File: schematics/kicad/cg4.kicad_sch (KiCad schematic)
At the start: 0 parts

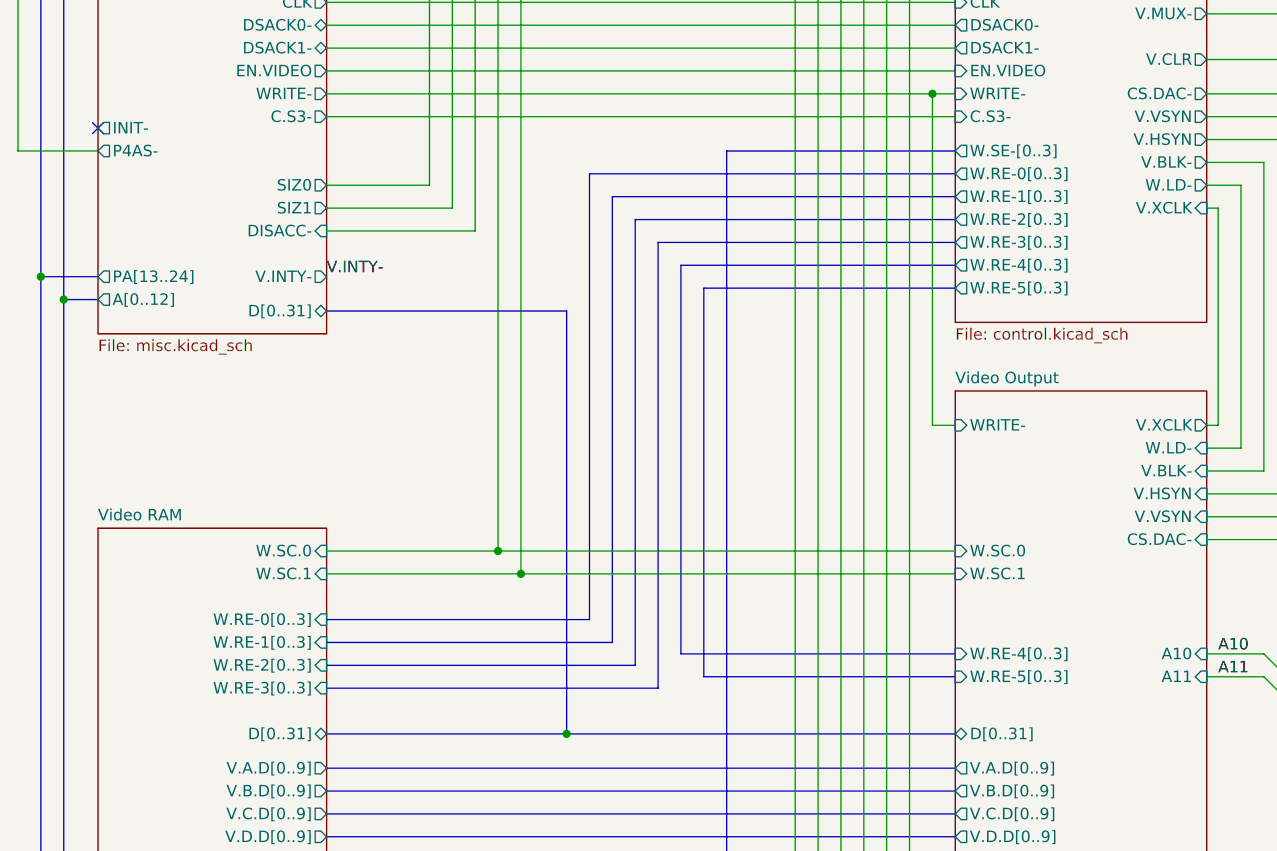
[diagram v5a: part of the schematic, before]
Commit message: Fix ERCs which uncovered some issues with W.RE for the overlay memory. Finish the ECL chips for clock control - need to find value of R1315. Add space for 0-ohm resistor on V.VSYN which exists in schematics but was never connected in the original composite sync scheme with 4 BNC connectors. Can leave it unconnected if it causes issues.
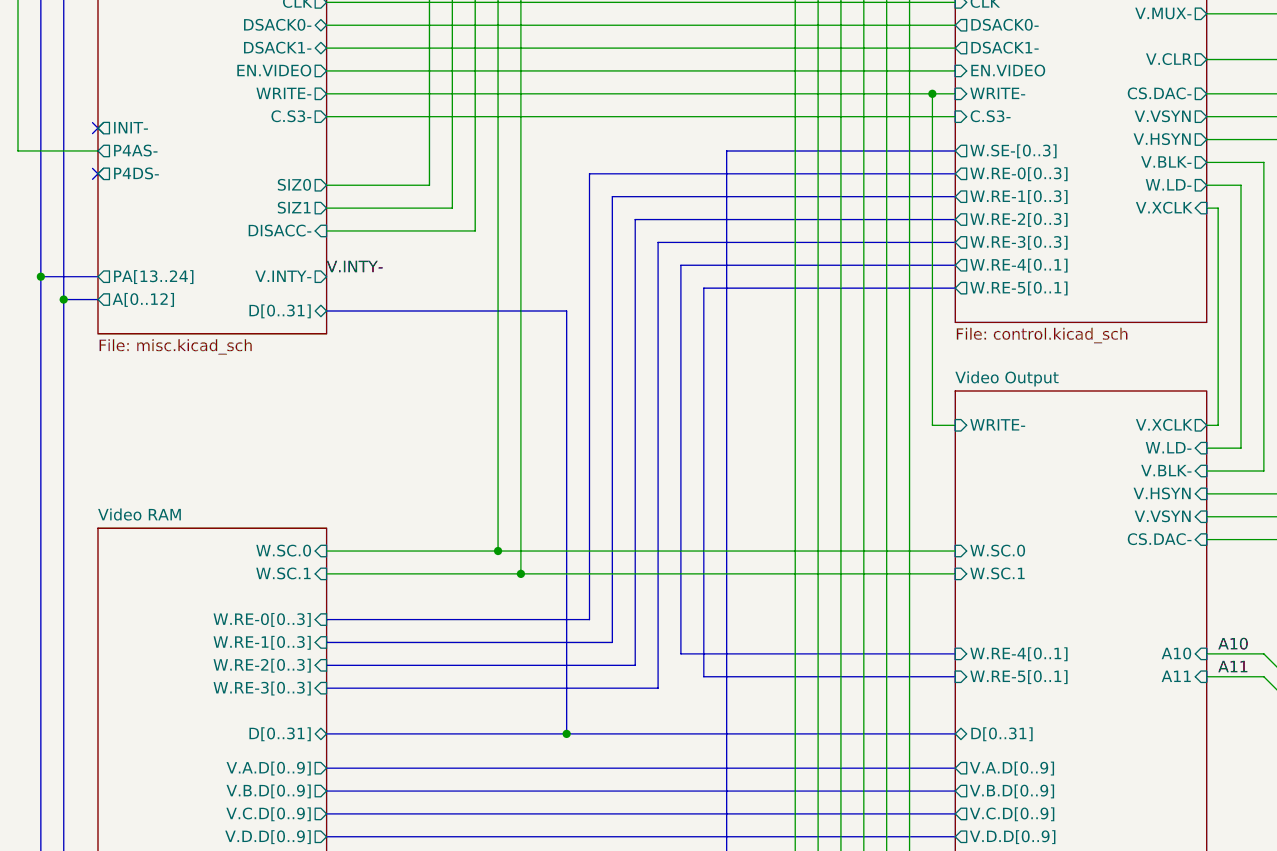
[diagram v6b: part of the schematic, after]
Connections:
- no-connect marks 1 -> 2
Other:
- sheet Misc ports: added P4DS-; removed none
- sheet Video Control ports: added W.RE-4[0..1], W.RE-5[0..1]; removed W.RE-4[0..3], W.RE-5[0..3]
- sheet Video Output ports: added W.RE-4[0..1], W.RE-5[0..1]; removed W.RE-4[0..3], W.RE-5[0..3]
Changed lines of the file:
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@@
 		(at 43.18 68.58)
+	)
+	(no_connect
+		(at 43.18 73.66)
 	)
 	(bus_entry
@@
 			)
 		)
-		(pin "W.RE-4[0..3]" output
+		(pin "W.RE-4[0..1]" output
 			(at 138.43 83.82 180)
 			(effects
@@
 			)
 		)
-		(pin "W.RE-5[0..3]" output
+		(pin "W.RE-5[0..1]" output
 			(at 138.43 86.36 180)
 			(effects
@@
 			)
 		)
+		(pin "P4DS-" output
+			(at 43.18 73.66 180)
+			(effects
+				(font
+					(size 1.27 1.27)
+				)
+				(justify left)
+			)
+		)
 		(instances
 			(project "cg4"
@@
 			)
 		)
-		(pin "W.RE-4[0..3]" input
+		(pin "W.RE-4[0..1]" input
 			(at 138.43 127 180)
 			(effects
@@
 			)
 		)
-		(pin "W.RE-5[0..3]" input
+		(pin "W.RE-5[0..1]" input
 			(at 138.43 129.54 180)
 			(effects
